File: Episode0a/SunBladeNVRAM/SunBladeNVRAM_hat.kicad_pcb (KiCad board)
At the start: 2 copper layers, 36.5 x 18.5 mm, 5 parts, among them J105 Conn_01x01_Pin, J106 Conn_01x01_Pin, J107 Conn_01x01_Pin, J108 Conn_01x01_Pin

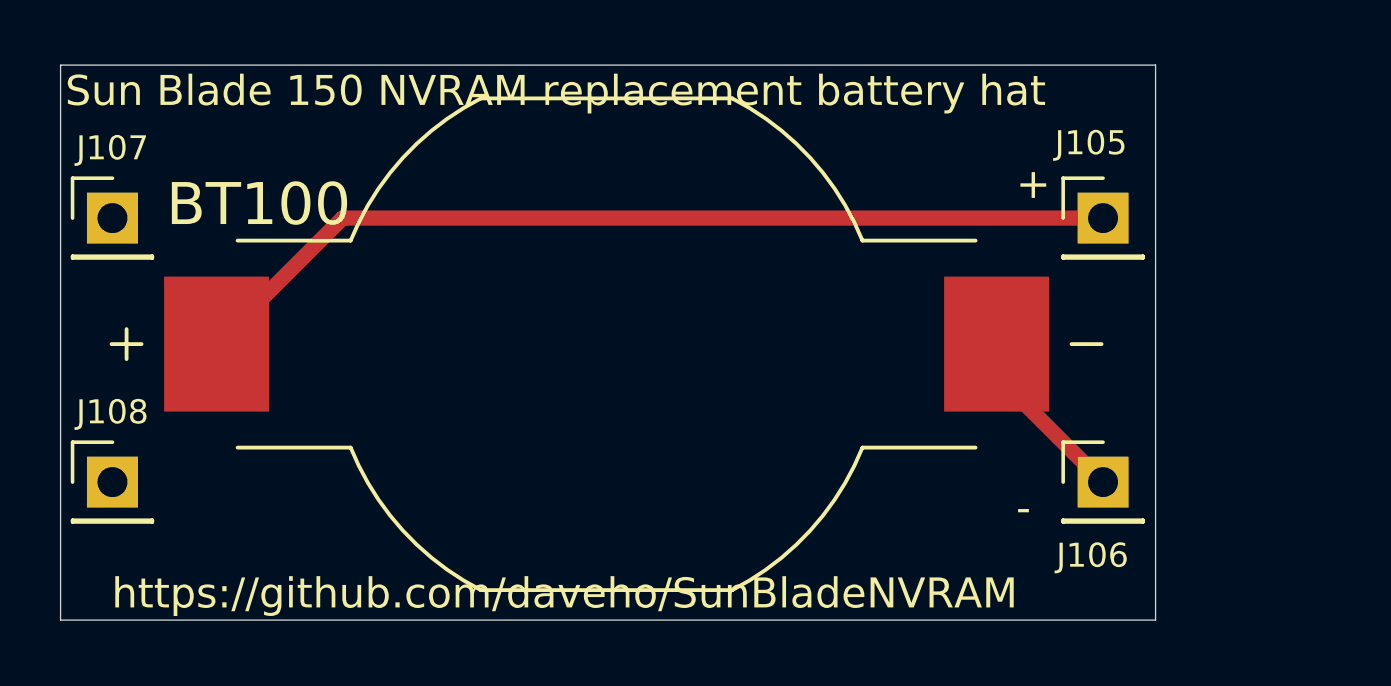
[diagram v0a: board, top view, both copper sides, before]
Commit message: remove xtal from bottom PCB
There's no point in wiring the xtal to the bottom PCB
since it can be soldered directly to the snap connectors
on the M48T59Y-70MH1.

Also, increase the size of the "notch" arc on the bottom
PCB, and add it to the top PCB.
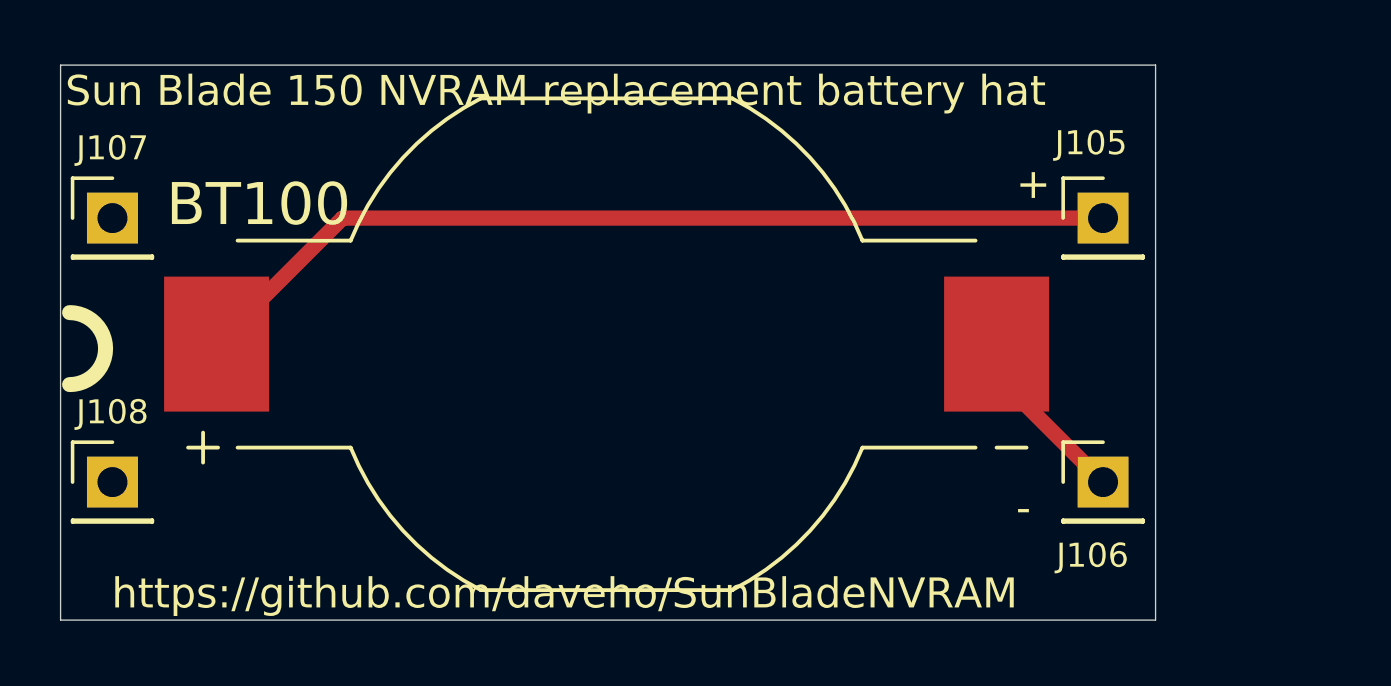
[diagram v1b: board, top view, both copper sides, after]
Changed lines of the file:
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@@
 		(attr smd)
 		(fp_line
-			(start -16.5 0)
-			(end -15.5 0)
-			(stroke
-				(width 0.127)
-				(type solid)
-			)
-			(layer "F.SilkS")
-		)
-		(fp_line
-			(start -16 -0.5)
-			(end -16 0.5)
+			(start -13.95 3.45)
+			(end -12.95 3.45)
+			(stroke
+				(width 0.127)
+				(type solid)
+			)
+			(layer "F.SilkS")
+		)
+		(fp_line
+			(start -13.45 2.95)
+			(end -13.45 3.95)
 			(stroke
 				(width 0.127)
@@
 		)
 		(fp_line
-			(start 15.5 0)
-			(end 16.5 0)
+			(start 13 3.45)
+			(end 14 3.45)
 			(stroke
 				(width 0.127)
@@
 		)
 	)
+	(gr_arc
+		(start 83.55 78.05)
+		(mid 84.75 79.25)
+		(end 83.55 80.45)
+		(stroke
+			(width 0.5)
+			(type default)
+		)
+		(layer "F.SilkS")
+	)
 	(gr_rect
